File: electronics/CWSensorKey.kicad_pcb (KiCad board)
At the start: 2 copper layers, 37 x 30 mm, 21 parts, among them J1 Tip, J2 GND, J3 Ring, J4 Dit, J5 Dah, J6 +, J7 -, Q1 IRFML8244TRPBF, Q2 IRFML8244TRPBF, U1 AT42QT1011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

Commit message: Branch (#3)
* index on main: b7a867d Further documentation in README.md Slightly changed dimensions of sensor pad Changed distance betw screws in sensor pad holder

* Adapted board for better fitting in the housing
Implemented script for generation of all 2D files from the KiCad models

* Delete electronics/gerbers directory

resolving merge conflict

* Update CWSensorKey.kicad_prl

updated active layer in kicad project file

---------

Co-authored-by: DL8ABG <dl8abg@qsl.net>
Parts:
- H1, H2, H3, H4: footprint MountingHole:MountingHole_2.7mm_M2.5_DIN965 -> MountingHole:MountingHole_3mm
- Q1, Q2: footprint Package_TO_SOT_SMD:SOT-23 -> Package_TO_SOT_SMD:SOT-23_Handsoldering
- moved R2 2.54 mm to (148.0, 101.6)
- moved J5 1.91 mm to (144.8, 97.8)
- moved J6 0.64 mm to (172.1, 103.5)
- moved J7 0.64 mm to (142.9, 103.5)
- moved J3 0.63 mm to (172.1, 99.1)
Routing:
- net +3.3V: track 62.5 -> 63.7 mm
- net Net-(J5-Pin_1): track 4.61 -> 5.61 mm
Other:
- outline, holes or cut-outs redrawn
- board text added: "Oct 2025"
- board text removed: "May 2025"

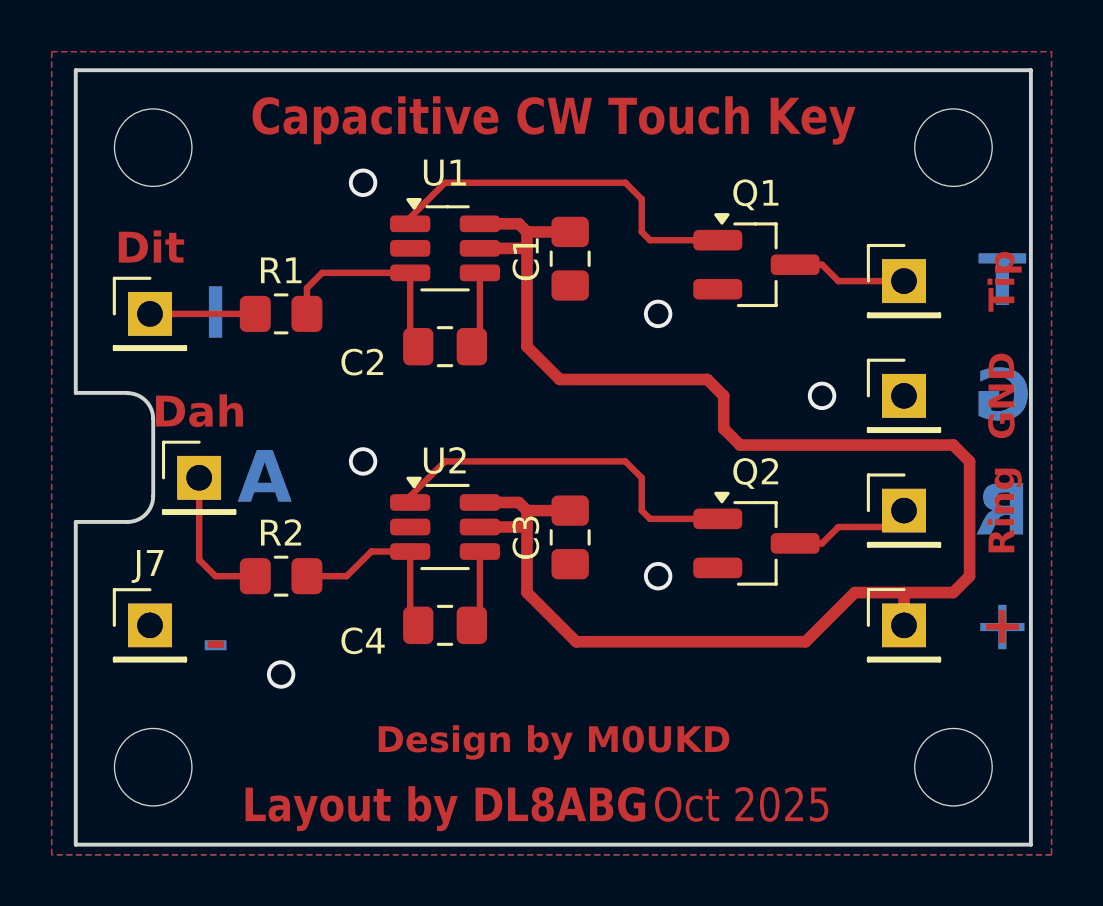
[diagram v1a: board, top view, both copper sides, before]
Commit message: - Changed SMD resistors and capacitors to 1206 as this size is available within the kit from AATIS - Added picture of the board for better overview on github
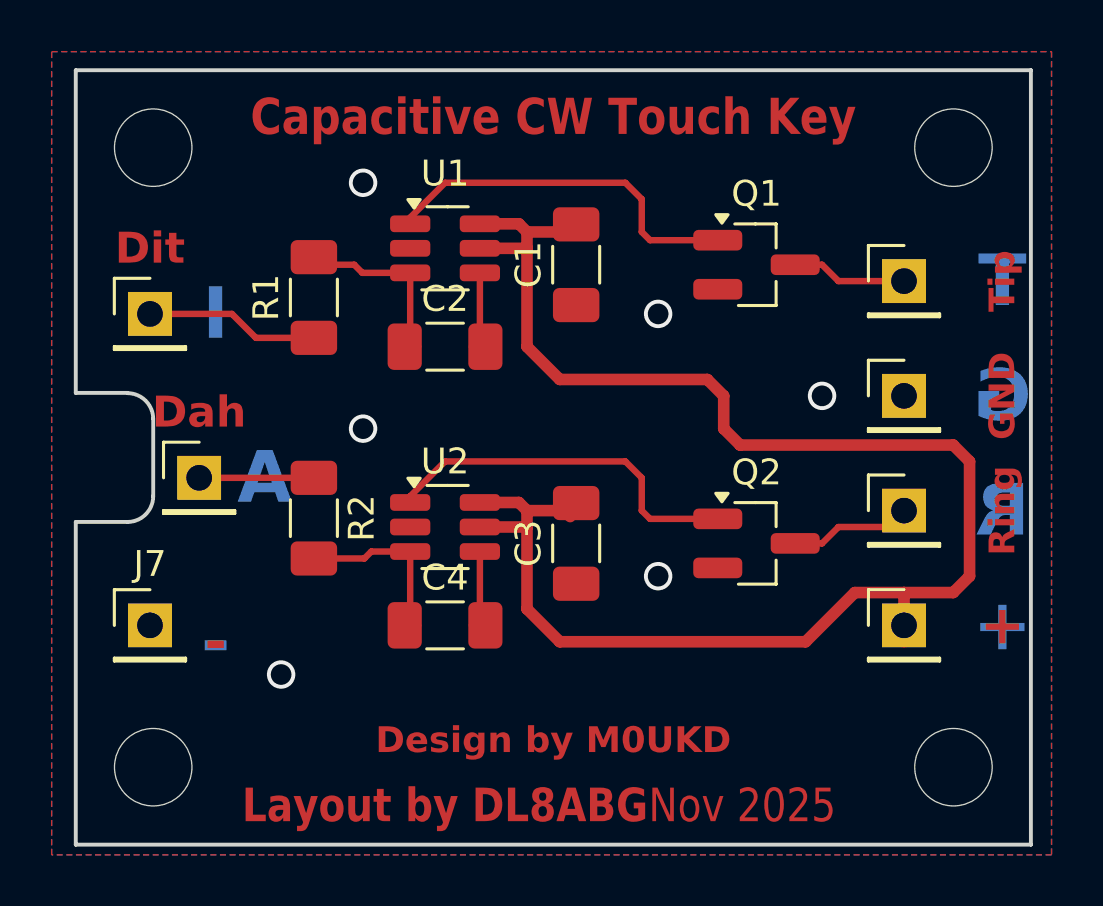
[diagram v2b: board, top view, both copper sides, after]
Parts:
- C1, C2, C3, C4: footprint Capacitor_SMD:C_0805_2012Metric_Pad1.18x1.45mm_HandSolder -> Capacitor_SMD:C_1206_3216Metric_Pad1.33x1.80mm_HandSolder
- R1, R2: footprint Resistor_SMD:R_0805_2012Metric_Pad1.20x1.40mm_HandSolder -> Capacitor_SMD:C_1206_3216Metric_Pad1.33x1.80mm_HandSolder
- moved R2 2.58 mm to (149.2, 99.4), turned to -90 degrees
- moved R1 1.42 mm to (149.2, 90.8), turned to 90 degrees
- moved C1 0.33 mm to (159.4, 89.5)
- moved C3 0.33 mm to (159.4, 100.3)
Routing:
- net Net-(J4-Pin_1): track 4.08 -> 6.73 mm
- net Net-(J5-Pin_1): track 5.61 -> 3.81 mm
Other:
- board text added: "Nov 2025"

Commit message: - added option for mounting battery holder to board with screw - added information on AATIS kit number
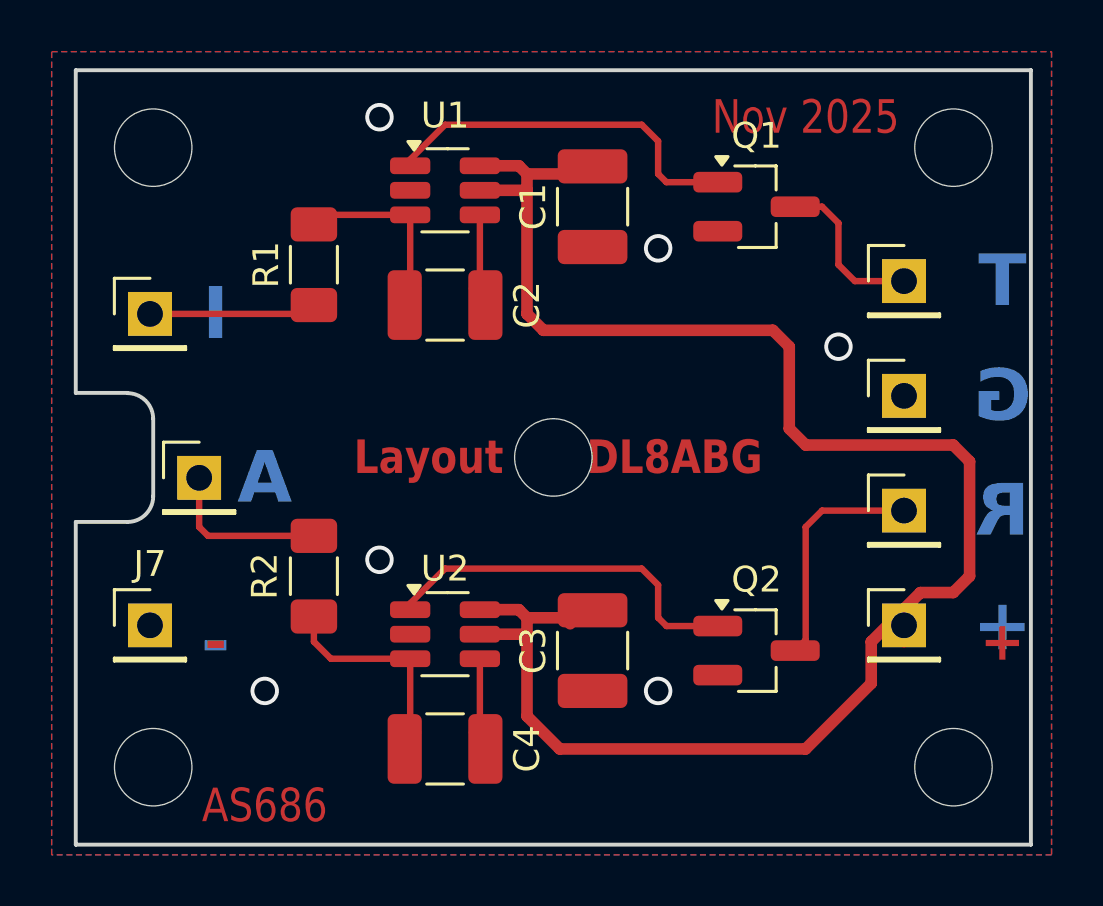
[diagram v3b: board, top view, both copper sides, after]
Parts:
- added H5: MountingHole, MountingHole:MountingHole_3mm, F.Cu at (158.5, 97.0)
- C1, C2, C3, C4: footprint Capacitor_SMD:C_1206_3216Metric_Pad1.33x1.80mm_HandSolder -> Capacitor_SMD:C_1210_3225Metric_Pad1.33x2.70mm_HandSolder
- moved C4 4.79 mm to (154.3, 108.3)
- moved C3 4.20 mm to (160.0, 104.5)
- moved Q2 4.15 mm to (166.4, 104.5)
- moved U2 4.15 mm to (154.3, 103.8)
- moved C1 2.34 mm to (160.0, 87.3)
- moved Q1 2.25 mm to (166.4, 87.3)
- moved U1 2.25 mm to (154.3, 86.7)
- moved R2 2.25 mm to (149.2, 101.6)
- moved C2 1.61 mm to (154.3, 91.1)
- moved R1 1.27 mm to (149.2, 89.5)
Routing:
- net +3.3V: track 64.1 -> 68.4 mm
- net Net-(J3-Pin_1): track 5.04 -> 9.03 mm
- net Net-(J5-Pin_1): track 3.81 -> 6.49 mm
- net Net-(J1-Pin_1): track 5.04 -> 6.92 mm
- net Net-(U2-SNSK): track 7.47 -> 7.97 mm
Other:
- board text added: "AS686"
- board text added: "DL8ABG"
- board text added: "Layout"
- board text removed: "Dah"
- board text removed: "Dit"
- board text removed: "GND"
- board text removed: "Layout by DL8ABG"
- board text removed: "Oct 2025"
- board text removed: "Ring"
- board text removed: "Tip"
